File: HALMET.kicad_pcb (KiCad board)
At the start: 4 copper layers, 89 x 58 mm, 226 parts, among them J1103 Conn_01x02, J1104 Conn_01x02, J1105 Conn_01x02, J1106 Conn_01x02, J201 GPIO, J203 Conn_01x01, J302 Conn_01x02, J401 USB_B_Micro, J602 Conn_02x04_Odd_Even, J604 Conn_01x02, J605 Conn_01x02, J606 Conn_01x02, J607 Conn_01x02, J702 Conn_01x04, J801 Conn_01x03, J802 Conn_01x04, Q401 S8050, Q402 S8050, Q601 S9015, Q602 S9015, Q603 S9015, Q604 S9015, SW501 SW_Push, SW502 SW_Push, U1101 74LVC1G17, U1102 74LVC1G17, U1103 74LVC1G17, U1104 74LVC1G17, U1201 π140U30, U1202 ISO1540, U1203 XC6206P332MR, U201 ESP32-WROOM-32, U202 XL1509-3.3, U401 CH340C, U501 SN65HVD230DR, U601 LMV324, U602 ADS1115IDGS

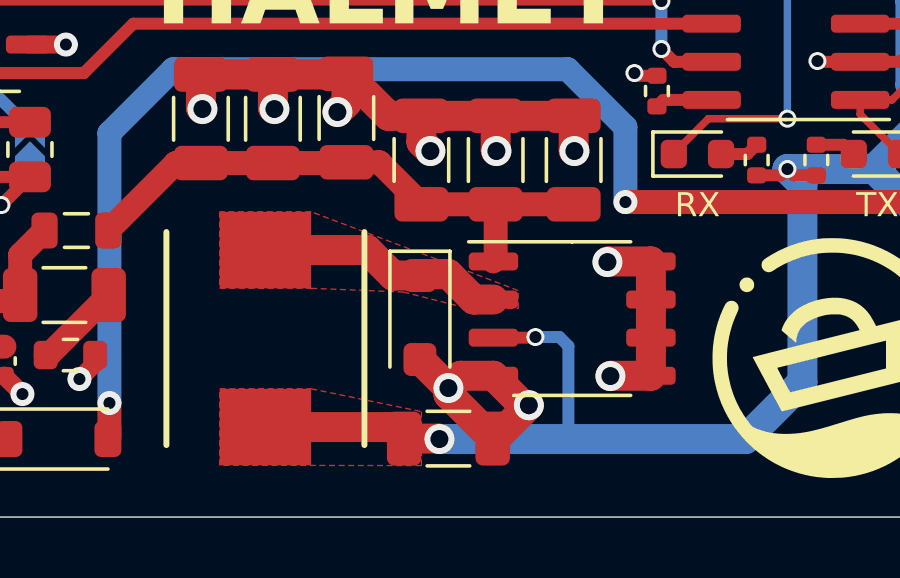
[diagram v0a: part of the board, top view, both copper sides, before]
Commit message: Update parts according to availability
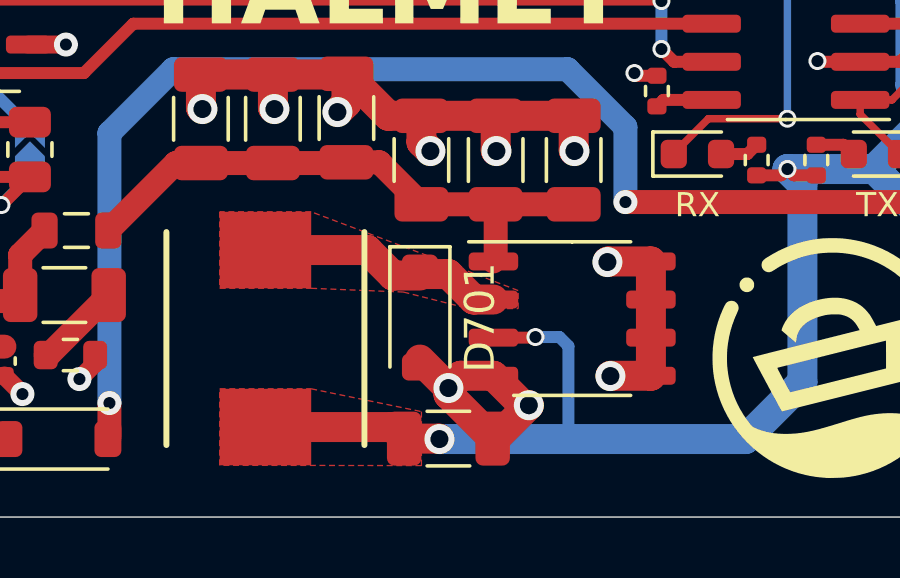
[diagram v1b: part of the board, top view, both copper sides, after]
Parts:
- C202: value 22uF/6.3V -> 22uF
- D701: footprint Diode_SMD:D_SOD-123F -> Diode_SMD:D_SOD-123
- L701: value CBC3225T100KR -> NLCV32T-100K-PFR
- U201: value ESP32-WROOM-32 -> ESP32-WROOM-32E-N16
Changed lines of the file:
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@@
         (effects (font (size 1 1) (thickness 0.15)))
     )
-    (fp_text value "22uF/6.3V" (at 0 1.43) (layer "F.Fab") hide
+    (fp_text value "22uF" (at 0 1.43) (layer "F.Fab") hide
         (effects (font (size 1 1) (thickness 0.15)))
     )
@@
     (tags "Single 2.4 GHz Wi-Fi and Bluetooth combo  chip")
     (property "JLCPCB_CORRECTION" "0;0;270")
-    (property "LCSC" "C701341")
+    (property "LCSC" "C701343")
     (property "Sheetfile" "ESP32.kicad_sch")
     (property "Sheetname" "ESP32")
@@
         (effects (font (size 1 1) (thickness 0.15)))
     )
-    (fp_text value "ESP32-WROOM-32" (at 0 11.5 90) (layer "F.Fab") hide
+    (fp_text value "ESP32-WROOM-32E-N16" (at 0 11.5 90) (layer "F.Fab") hide
         (effects (font (size 1 1) (thickness 0.15)))
     )
@@
     (descr "Inductor SMD 1210 (3225 Metric), square (rectangular) end terminal, IPC_7351 nominal, (Body size source: http://www.tortai-tech.com/upload/download/2011102023233369053.pdf), generated with kicad-footprint-generator")
     (tags "inductor")
-    (property "LCSC" "C90321")
+    (property "LCSC" "C74563")
     (property "Notes" "Alternative: CBC3225T100KR")
     (property "Part" "")
@@
         (effects (font (size 1 1) (thickness 0.15)))
     )
-    (fp_text value "CBC3225T100KR" (at 0 2.28 90) (layer "F.Fab") hide
+    (fp_text value "NLCV32T-100K-PFR" (at 0 2.28 90) (layer "F.Fab") hide
         (effects (font (size 1 1) (thickness 0.15)))
     )
@@
     )
   )
-  (footprint "Diode_SMD:D_SOD-123F" (layer "F.Cu")
+  (footprint "Diode_SMD:D_SOD-123" (layer "F.Cu")
     (at 124.85 108.35 -90)
-    (descr "D_SOD-123F")
-    (tags "D_SOD-123F")
+    (descr "SOD-123")
+    (tags "SOD-123")
     (property "LCSC" "C8598")
     (property "Notes" "")
@@
     (property "ki_keywords" "diode Schottky")
     (attr smd)
-    (fp_text reference "D701" (at -0.127 -1.905 90) (layer "F.SilkS") hide
+    (fp_text reference "D701" (at 0 -2 -90) (layer "F.SilkS")
         (effects (font (size 1 1) (thickness 0.15)))
     )
-    (fp_text value "B5819W" (at 0 2.1 90) (layer "F.Fab") hide
+    (fp_text value "B5819W" (at 0 2.1 -90) (layer "F.Fab")
         (effects (font (size 1 1) (thickness 0.15)))
     )
-    (fp_text user "${REFERENCE}" (at -0.127 -1.905 90) (layer "F.Fab") hide
+    (fp_text user "${REFERENCE}" (at 0 -2 -90) (layer "F.Fab")
         (effects (font (size 1 1) (thickness 0.15)))
     )
-    (fp_line (start -2.21 -1) (end -2.21 1)
+    (fp_line (start -2.36 -1) (end -2.36 1)
       (stroke (width 0.12) (type solid)) (layer "F.SilkS"))
-    (fp_line (start -2.21 -1) (end 1.65 -1)
+    (fp_line (start -2.36 -1) (end 1.65 -1)
       (stroke (width 0.12) (type solid)) (layer "F.SilkS"))
-    (fp_line (start -2.21 1) (end 1.65 1)
+    (fp_line (start -2.36 1) (end 1.65 1)
       (stroke (width 0.12) (type solid)) (layer "F.SilkS"))
-    (fp_line (start -2.2 -1.15) (end -2.2 1.15)
+    (fp_line (start -2.35 -1.15) (end -2.35 1.15)
       (stroke (width 0.05) (type solid)) (layer "F.CrtYd"))
-    (fp_line (start -2.2 -1.15) (end 2.2 -1.15)
+    (fp_line (start -2.35 -1.15) (end 2.35 -1.15)
       (stroke (width 0.05) (type solid)) (layer "F.CrtYd"))
-    (fp_line (start 2.2 -1.15) (end 2.2 1.15)
+    (fp_line (start 2.35 -1.15) (end 2.35 1.15)
       (stroke (width 0.05) (type solid)) (layer "F.CrtYd"))
-    (fp_line (start 2.2 1.15) (end -2.2 1.15)
+    (fp_line (start 2.35 1.15) (end -2.35 1.15)
       (stroke (width 0.05) (type solid)) (layer "F.CrtYd"))
     (fp_line (start -1.4 -0.9) (end 1.4 -0.9)
@@
     (fp_line (start 1.4 0.9) (end -1.4 0.9)
       (stroke (width 0.1) (type solid)) (layer "F.Fab"))
-    (pad "1" smd roundrect (at -1.4 0 270) (size 1.1 1.1) (layers "F.Cu" "F.Paste" "F.Mask") (roundrect_rratio 0.2272727273)
+    (pad "1" smd roundrect (at -1.65 0 270) (size 0.9 1.2) (layers "F.Cu" "F.Paste" "F.Mask") (roundrect_rratio 0.25)
       (net 6 "/Power input/SW") (pinfunction "K") (pintype "passive"))
-    (pad "2" smd roundrect (at 1.4 0 270) (size 1.1 1.1) (layers "F.Cu" "F.Paste" "F.Mask") (roundrect_rratio 0.2272727273)
+    (pad "2" smd roundrect (at 1.65 0 270) (size 0.9 1.2) (layers "F.Cu" "F.Paste" "F.Mask") (roundrect_rratio 0.25)
       (net 1 "GND") (pinfunction "A") (pintype "passive"))
-    (model "${KICAD6_3DMODEL_DIR}/Diode_SMD.3dshapes/D_SOD-123F.wrl"
+    (model "${KICAD6_3DMODEL_DIR}/Diode_SMD.3dshapes/D_SOD-123.wrl"
       (offset (xyz 0 0 0))
       (scale (xyz 1 1 1))
@@
   (gr_text "HALMET" (at 145.25 89.225) (layer "B.SilkS" knockout)
     (effects (font (face "IBM Plex Sans Medm") (size 2.5 2.5) (thickness 0.5) bold) (justify left bottom mirror))
-    (render_cache "HALMET" -0
+    (render_cache "HALMET" 0
       (polygon
         (pts

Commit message: Fix DI4 & DI3 pins
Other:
- board text added: "26 DI4"
- board text added: "27 DI3"
- board text removed: "26 DI3"
- board text removed: "27 DI4"
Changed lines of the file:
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@@
     (effects (font (size 0.8 0.8) (thickness 0.15) bold) (justify mirror))
   )
-  (gr_text "27   DI4" (at 162.85 96.5) (layer "B.SilkS")
+  (gr_text "27   DI3" (at 162.85 96.5) (layer "B.SilkS")
     (effects (font (size 0.8 0.8) (thickness 0.16)) (justify left mirror))
   )
@@
     (effects (font (size 0.8 0.8) (thickness 0.15) bold) (justify bottom mirror))
   )
-  (gr_text "26   DI3" (at 162.85 95.35) (layer "B.SilkS")
+  (gr_text "26   DI4" (at 162.85 95.35) (layer "B.SilkS")
     (effects (font (size 0.8 0.8) (thickness 0.16)) (justify left mirror))
   )

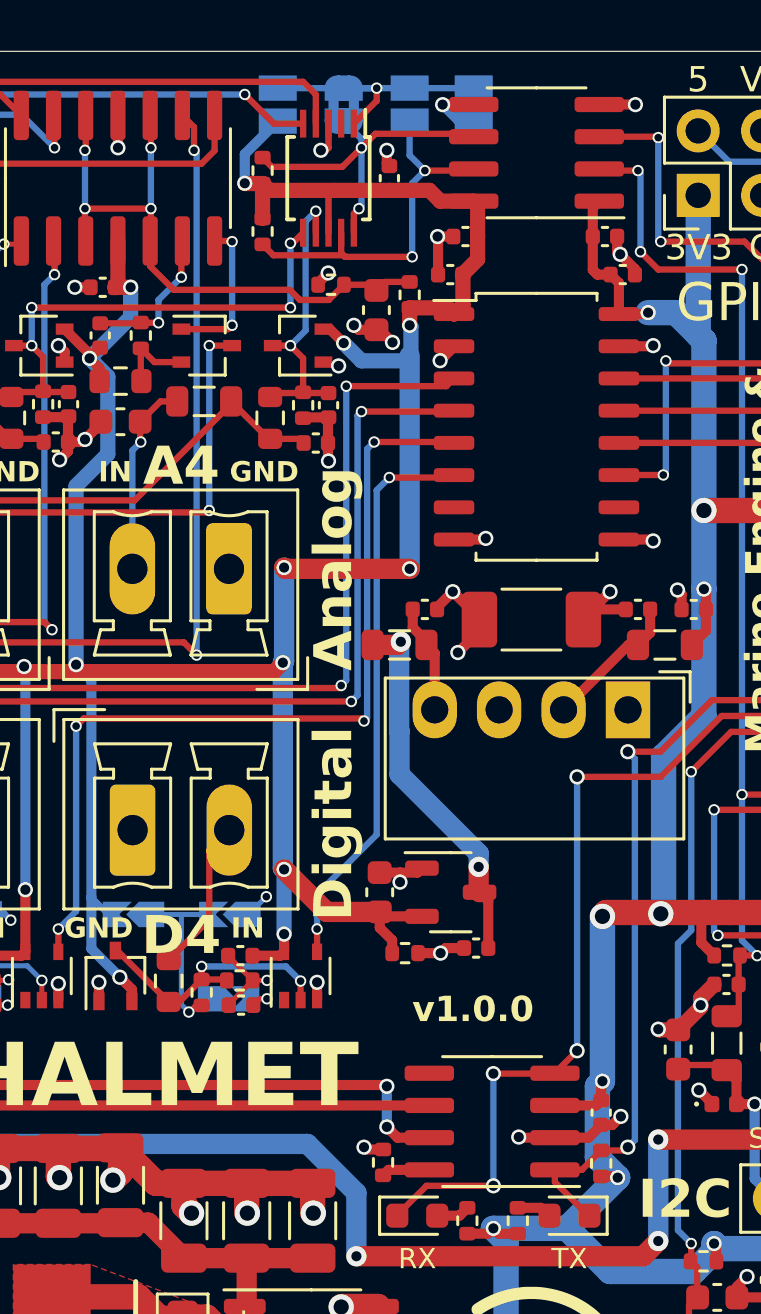
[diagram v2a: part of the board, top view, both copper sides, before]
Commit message: Version 1.0.1 changes
- Add a power header to isolated side
- Fix GPIO silk screen bugs
- Add labels for isolated I2C pads
- Bump version to 1.0.1
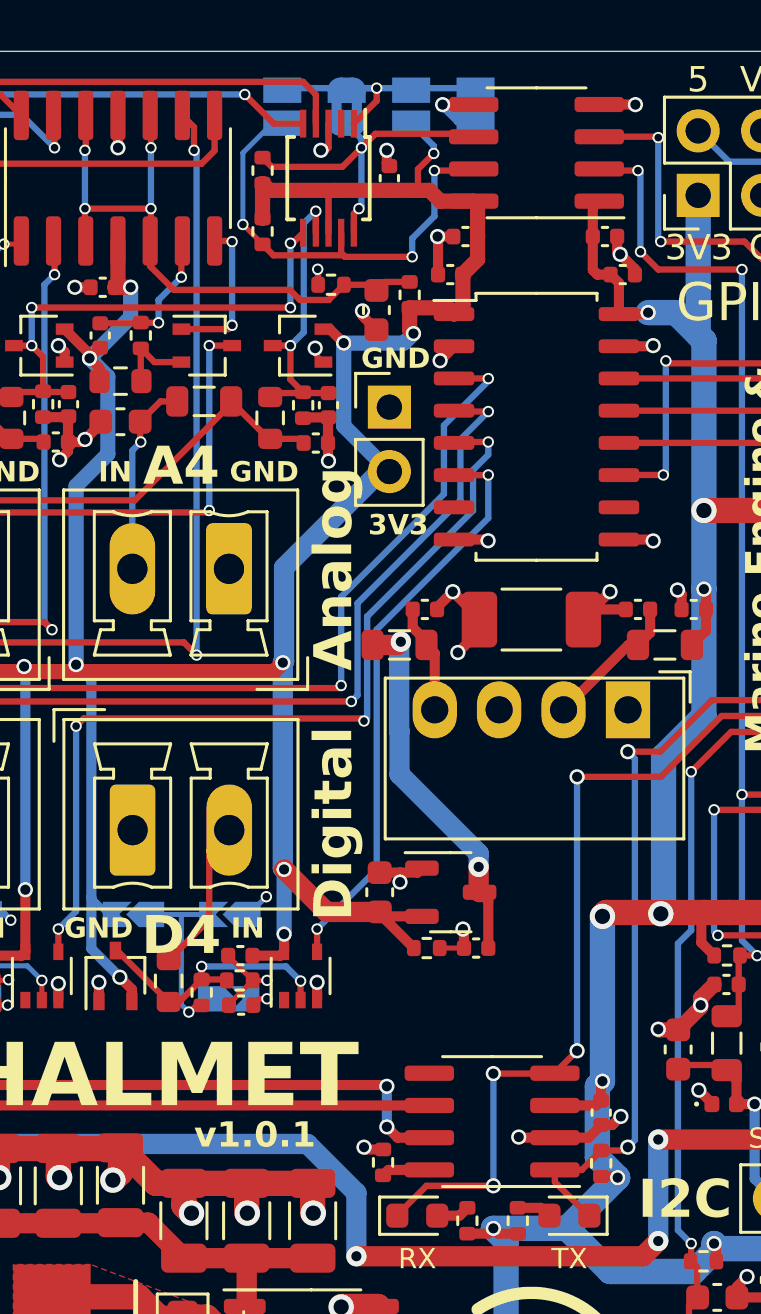
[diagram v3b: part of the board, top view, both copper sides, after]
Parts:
- added J1201: Conn_01x02, Connector_PinHeader_2.54mm:PinHeader_1x02_P2.54mm_Vertical, F.Cu at (133.0, 71.0)
- moved JP602 5.26 mm to (133.9, 59.2)
- moved JP604 5.02 mm to (128.8, 59.2)
- moved R1201 0.88 mm to (134.5, 92.3)
- moved JP603 0.14 mm to (131.3, 59.2)
- moved JP605 0.11 mm to (136.4, 59.2)
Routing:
- net /Analog input/SDA: track 14.8 -> 18.2 mm, vias 2 -> 3
- net +3.3V_1: track 253.0 -> 250.0 mm, vias 25 -> 23
- net /Digital input/DigIn4: track 22.3 -> 23.1 mm
- net GND1: track 63.7 -> 63.6 mm, vias 42 -> 41
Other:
- board text added: "v1.0.1"
- board text removed: "https://github.com/hatlabs/HALBET-hardware/"
- board text removed: "v1.0.0"

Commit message: Update parts according to availability
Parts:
- F401: value ASMD1206-050 -> BSMD1206-100-6V
- L701: value NLCV32T-100K-PFR -> NLCV32T-100K-EFR
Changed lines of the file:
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@@
     (tags "LED")
     (property "JLCPCB_CORRECTION" "")
-    (property "LCSC" "C72041")
+    (property "LCSC" "C84266")
     (property "Sheetfile" "UI.kicad_sch")
     (property "Sheetname" "User Interface")
@@
     (tags "fuse")
     (property "JLCPCB_CORRECTION" "")
-    (property "LCSC" "C135338")
+    (property "LCSC" "C883129")
     (property "Sheetfile" "USB.kicad_sch")
     (property "Sheetname" "USB")
@@
         (effects (font (size 1 1) (thickness 0.15)))
     )
-    (fp_text value "ASMD1206-050" (at 0 1.82 90) (layer "F.Fab") hide
+    (fp_text value "BSMD1206-100-6V" (at 0 1.82 90) (layer "F.Fab") hide
         (effects (font (size 1 1) (thickness 0.15)))
     )
@@
     (tags "SOT-323 SC-70")
     (property "JLCPCB_CORRECTION" "0;0;180")
-    (property "LCSC" "C134404")
+    (property "LCSC" "C78261")
     (property "Sheetfile" "ESP32.kicad_sch")
     (property "Sheetname" "ESP32")
@@
     (tags "SOT-323 SC-70")
     (property "JLCPCB_CORRECTION" "0;0;180")
-    (property "LCSC" "C134404")
+    (property "LCSC" "C78261")
     (property "Sheetfile" "ESP32.kicad_sch")
     (property "Sheetname" "ESP32")
@@
     (descr "Capacitor SMD 1812 (4532 Metric), square (rectangular) end terminal, IPC_7351 nominal, (Body size source: IPC-SM-782 page 76, https://www.pcb-3d.com/wordpress/wp-content/uploads/ipc-sm-782a_amendment_1_and_2.pdf), generated with kicad-footprint-generator")
     (tags "capacitor")
-    (property "LCSC" "C1021634")
+    (property "LCSC" "C2940747")
     (property "Sheetfile" "isolation.kicad_sch")
     (property "Sheetname" "Isolation barrier")
@@
     (descr "LED SMD 0603 (1608 Metric), square (rectangular) end terminal, IPC_7351 nominal, (Body size source: http://www.tortai-tech.com/upload/download/2011102023233369053.pdf), generated with kicad-footprint-generator")
     (tags "LED")
-    (property "LCSC" "C72043")
+    (property "LCSC" "C965804")
     (property "Sheetfile" "UI.kicad_sch")
     (property "Sheetname" "User Interface")
@@
     (property "ki_description" "Generic connector, single row, 01x02, script generated (kicad-library-utils/schlib/autogen/connector/)")
     (property "ki_keywords" "connector")
-    (attr through_hole exclude_from_pos_files exclude_from_bom)
+    (attr through_hole exclude_from_pos_files)
     (fp_text reference "J1201" (at 0 -2.33) (layer "F.SilkS") hide
         (effects (font (size 1 1) (thickness 0.15)))
@@
     (descr "Inductor SMD 1210 (3225 Metric), square (rectangular) end terminal, IPC_7351 nominal, (Body size source: http://www.tortai-tech.com/upload/download/2011102023233369053.pdf), generated with kicad-footprint-generator")
     (tags "inductor")
-    (property "LCSC" "C74563")
+    (property "LCSC" "C295195")
     (property "Notes" "Alternative: CBC3225T100KR")
     (property "Part" "")
@@
         (effects (font (size 1 1) (thickness 0.15)))
     )
-    (fp_text value "NLCV32T-100K-PFR" (at 0 2.28 90) (layer "F.Fab") hide
+    (fp_text value "NLCV32T-100K-EFR" (at 0 2.28 90) (layer "F.Fab") hide
         (effects (font (size 1 1) (thickness 0.15)))
     )
@@
     (descr "LED SMD 0603 (1608 Metric), square (rectangular) end terminal, IPC_7351 nominal, (Body size source: http://www.tortai-tech.com/upload/download/2011102023233369053.pdf), generated with kicad-footprint-generator")
     (tags "LED")
-    (property "LCSC" "C72043")
+    (property "LCSC" "C965804")
     (property "Sheetfile" "UI.kicad_sch")
     (property "Sheetname" "User Interface")
@@
     (effects (font (size 0.8 0.8) (thickness 0.15) bold) (justify mirror))
   )
+  (gr_text "3V3" (at 135.3 73.2) (layer "B.SilkS")
+    (effects (font (size 0.8 0.8) (thickness 0.15) bold) (justify top mirror))
+  )
   (gr_text "A4" (at 124.8 74) (layer "B.SilkS")
     (effects (font (size 1.5 1.5) (thickness 0.25) bold) (justify mirror))
@@
     (effects (font (size 1 1) (thickness 0.16)) (justify top mirror))
   )
+  (gr_text "GND" (at 135.4 71.5) (layer "B.SilkS")
+    (effects (font (size 0.8 0.8) (thickness 0.15) bold) (justify bottom mirror))
+  )
   (gr_text "IN" (at 106.3 85.1) (layer "B.SilkS")
